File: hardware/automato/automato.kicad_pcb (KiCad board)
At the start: 2 copper layers, 100 x 90 mm, 86 parts, among them J1 Motor1, J10 Servo 3, J11 Servo 4, J12 Barrel_Jack, J2 Motor2, J3 Motor4, J4 Motor3, J5 Servo 1, J6 i2c, J7 Servo 2, J8 Relay 1, J9 Relay 2, K1 G5Q-1A, K2 G5Q-1A, Q1 AO3400A, Q2 AO3400A, Q3 AO3400A, Q4 AO3400A, Q5 AO3400A, Q6 AO3400A, Q7 HY12P03C2, U1 ESP32-C6-DEVKITC-1-N8, U6 TPS5450DDAR

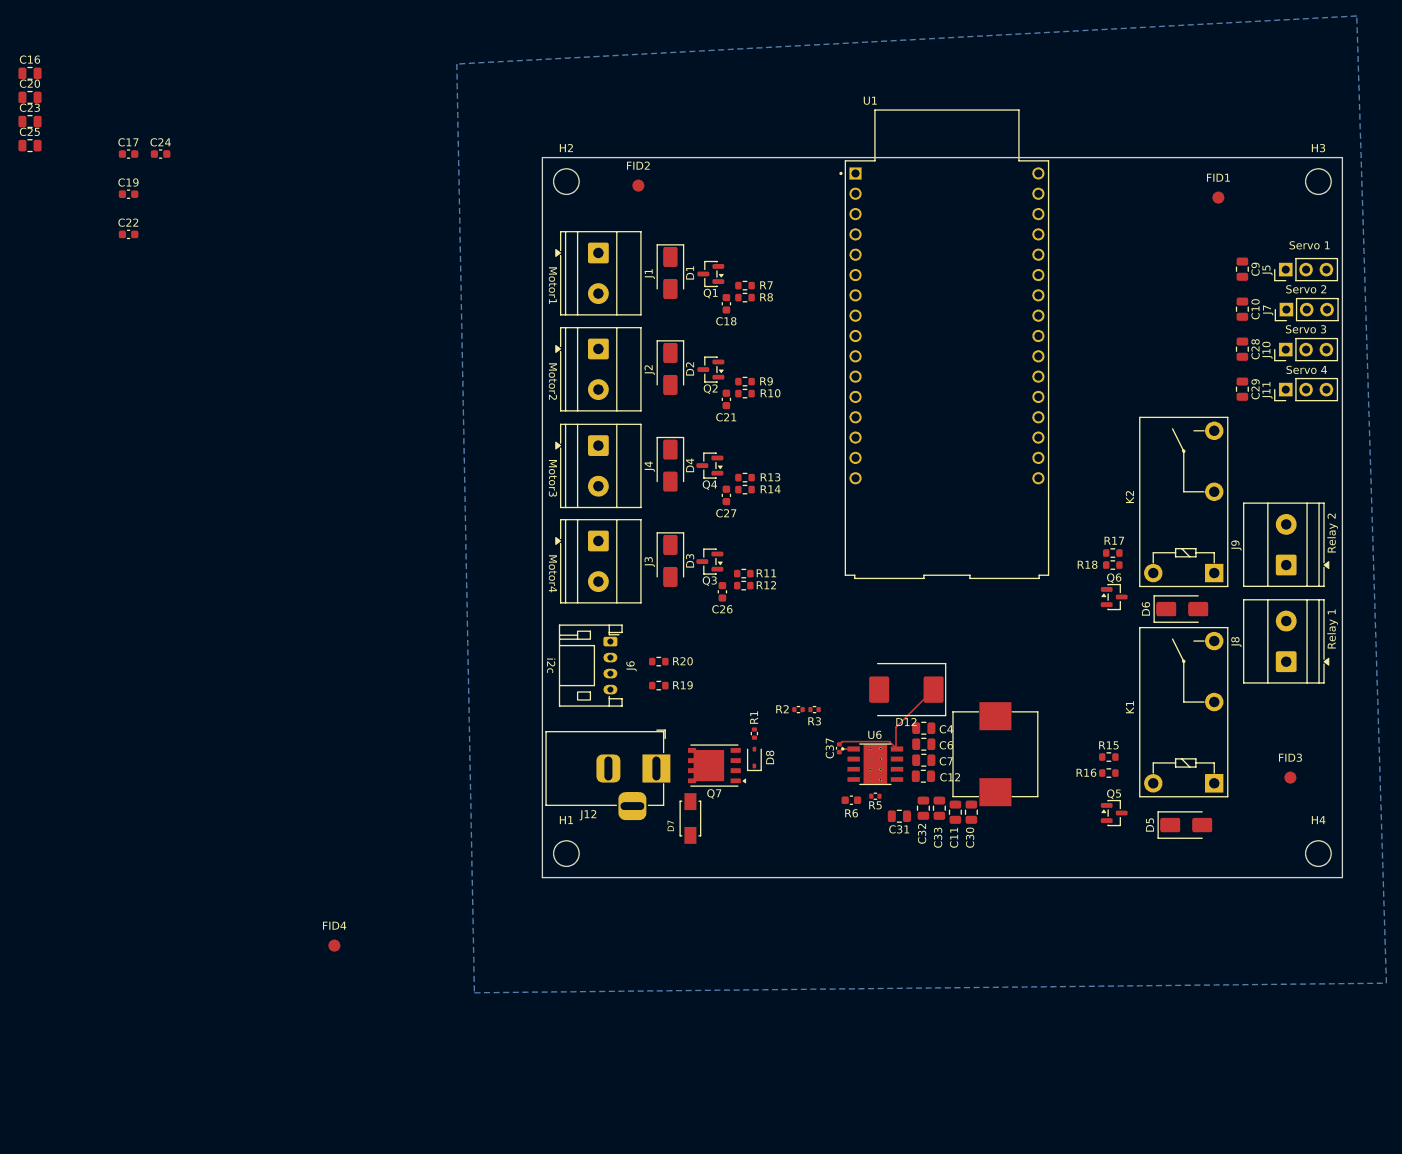
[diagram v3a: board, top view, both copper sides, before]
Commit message: sent to production
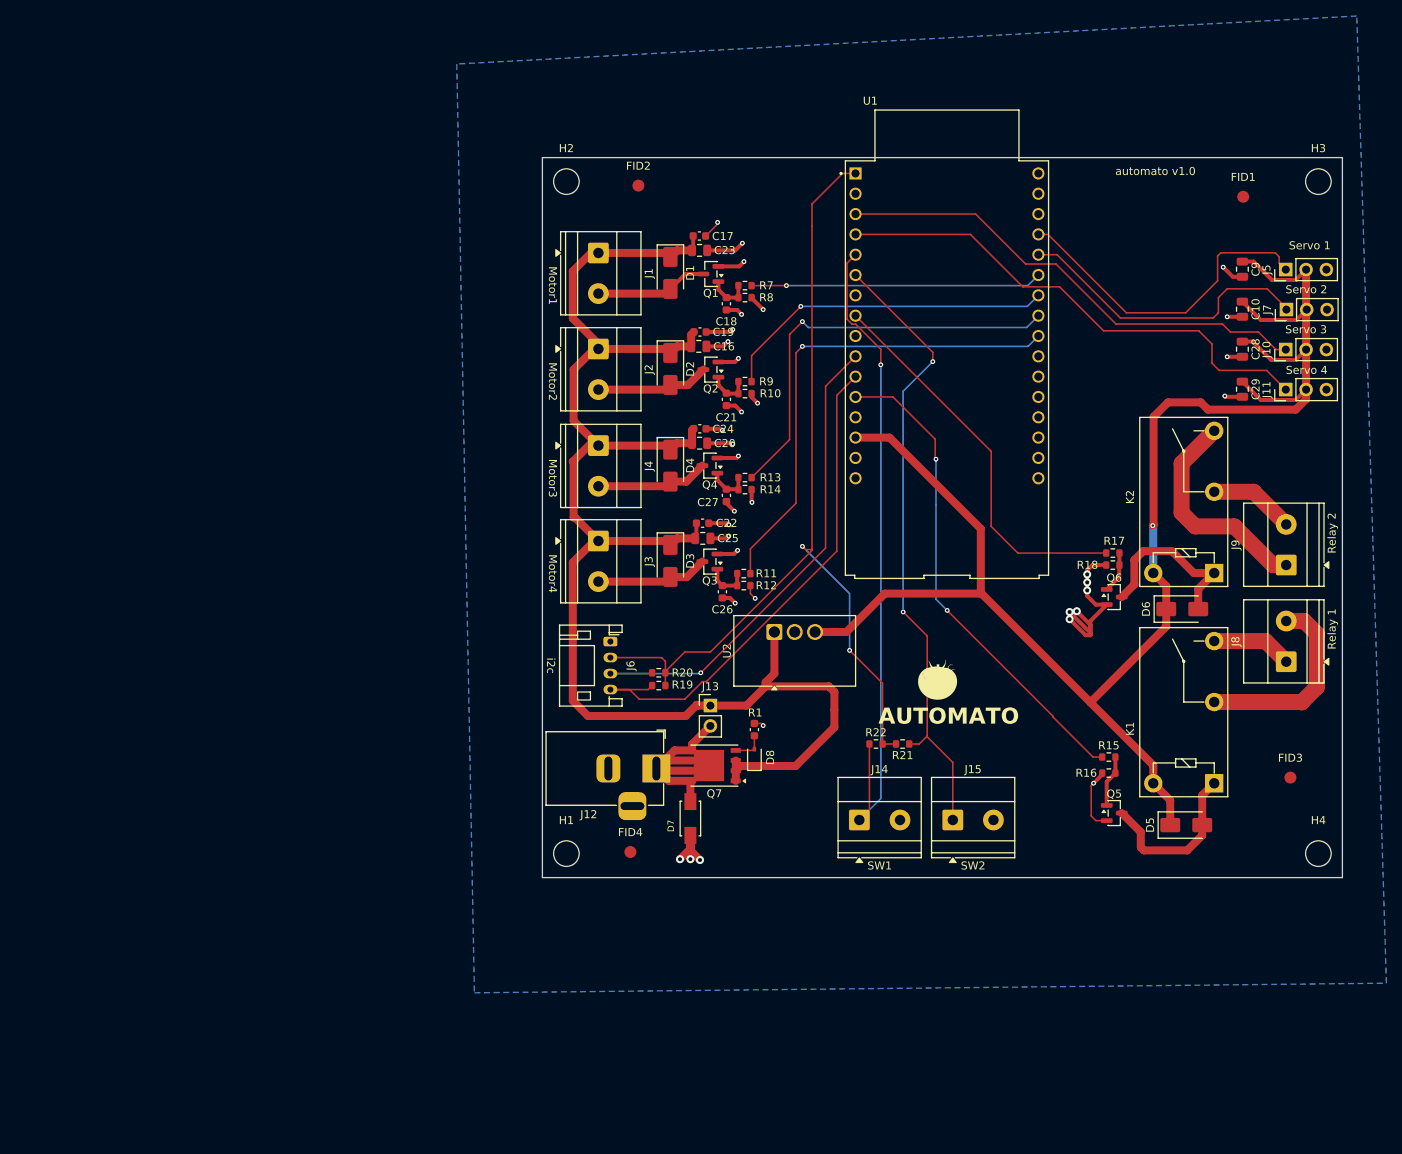
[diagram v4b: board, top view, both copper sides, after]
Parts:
- removed C11, C30, C31, C32, C33: 47uF, Capacitor_SMD:C_0805_2012Metric
- removed C12, C4, C6, C7: 2.2uF, Capacitor_SMD:C_0805_2012Metric
- removed C37: 10nF (LOW ESR), Capacitor_SMD:C_0402_1005Metric
- removed D12: SM540C, Diode_SMD:D_SMC
- removed L4: 15uH, BlackPanda:L_10.5x11.5_H4.0
- removed R2: 1K, Resistor_SMD:R_0402_1005Metric
- removed R3: 10K, Resistor_SMD:R_0402_1005Metric
- removed R5: 10K (1%), Resistor_SMD:R_0402_1005Metric
- removed R6: 3.16K (1%), Capacitor_SMD:C_0603_1608Metric
- removed U6: TPS5450DDAR, BlackPanda:CONV_TPS5450DDAR
- added G***: LOGO, LOGO, F.Cu at (198.4, 107.4)
- added J13: 12V Bypass, Connector_PinHeader_2.54mm:PinHeader_1x02_P2.54mm_Vertical, F.Cu at (170.0, 110.5)
- added J14: SW1, TerminalBlock_Phoenix:TerminalBlock_Phoenix_MKDS-1,5-2-5.08_1x02_P5.08mm_Horizontal, F.Cu at (188.6, 124.8)
- added J15: SW2, TerminalBlock_Phoenix:TerminalBlock_Phoenix_MKDS-1,5-2-5.08_1x02_P5.08mm_Horizontal, F.Cu at (200.3, 124.8)
- added R21: 10k, Resistor_SMD:R_0603_1608Metric, F.Cu at (194.0, 115.3)
- added R22: 10k, Resistor_SMD:R_0603_1608Metric, F.Cu at (190.7, 115.3)
- added U2: TSR2-2450N, Converter_DCDC:Converter_DCDC_TRACO_TSR2-24xxN_TSR2-24xxxN_THT, F.Cu at (178.0, 101.3)
- K1, K2: value G5Q-1A -> G5Q-1A-DC5
- R1: footprint Resistor_SMD:R_0402_1005Metric -> Capacitor_SMD:C_0603_1608Metric
- R19, R20: value 4.7k -> 2.2k
- moved C25 97.4 mm to (169.1, 89.6)
- moved C20 94.2 mm to (168.7, 77.7)
- moved C16 90.3 mm to (168.6, 65.6)
- moved C23 85.2 mm to (168.7, 53.6)
- moved C22 80.3 mm to (169.0, 87.7)
- moved C24 75.6 mm to (168.7, 75.9)
- moved C19 73.5 mm to (168.7, 63.8)
- moved C17 72.1 mm to (168.6, 51.8)
- moved FID4 38.8 mm to (160.0, 128.8)
- moved FID1 3.10 mm to (236.6, 46.9)
- moved R20 1.40 mm to (163.5, 106.4), turned to 0 degrees
- moved R1 0.50 mm to (175.5, 113.5)
- turned R19 to 0 degrees
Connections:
- U1 pad J1_5: VoltageSens -> SW1
- U1 pad J1_6: unconnected-(U1-GPIO5-PadJ1_6) -> SW2
- U1 pad J1_7: RELAY_1 -> unconnected-(U1-GPIO0-PadJ1_7)
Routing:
- net +5V: track 0.00 -> 205.3 mm, vias 0 -> 1
- net +12V: track 0.00 -> 188.5 mm
- net +3.3V: track 0.00 -> 117.1 mm, vias 0 -> 2
- net GND: track 0.00 -> 103.2 mm, vias 0 -> 35
- net SW1: track 0.00 -> 84.3 mm, vias 0 -> 1
- net SW2: track 0.00 -> 78.9 mm, vias 0 -> 2
- net SCL: track 0.00 -> 64.7 mm
- net SDA: track 0.00 -> 64.2 mm, vias 0 -> 1
- net SERVO_4: track 0.00 -> 63.2 mm
- net RELAY_1: track 0.00 -> 61.2 mm, vias 0 -> 2
- net MOTOR_4: track 0.00 -> 61.1 mm, vias 0 -> 1
- net SERVO_3: track 0.00 -> 60.8 mm
- net MOTOR_3: track 0.00 -> 52.5 mm, vias 0 -> 1
- net RELAY_2: track 0.00 -> 49.1 mm
- net MOTOR_2: track 0.00 -> 42.2 mm, vias 0 -> 1
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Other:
- board text added: "AUTOMATO"
- board text added: "automato v1.0"
